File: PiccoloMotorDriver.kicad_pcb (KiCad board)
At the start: 6 copper layers, 55 x 50 mm, 127 parts, among them J1 01x03_MotorTerminal, J11 CAN, J2 Debug, J3 RS485, J4 Conn_01x05, J5 Screw_Terminal_01x02_POWER, J6 Connector, USB-TYPE-C-16P, J7 Conn_01x05, J8 AUX0, J9 AUX0, U1 SP485EEN, U2 XC6210B332MR, U3 XL1509, U4 TJA1050T/CM,118, U5 AS5047D, U6 USBLC6-2SC6, U7 STM32H723VGHx, U8 DRV8316RRGFR, X2 X322516MLB4SI

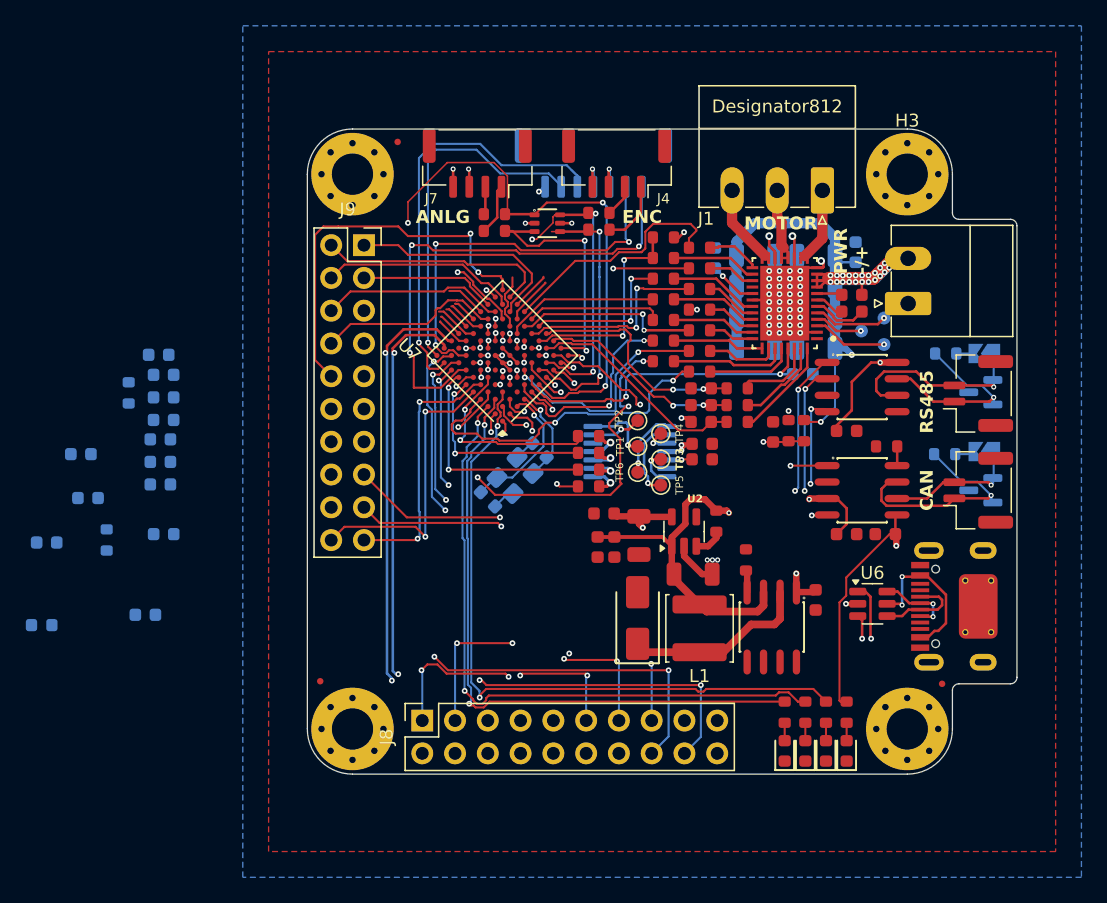
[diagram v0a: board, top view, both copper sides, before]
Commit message: Finished layout, pcba is being tested
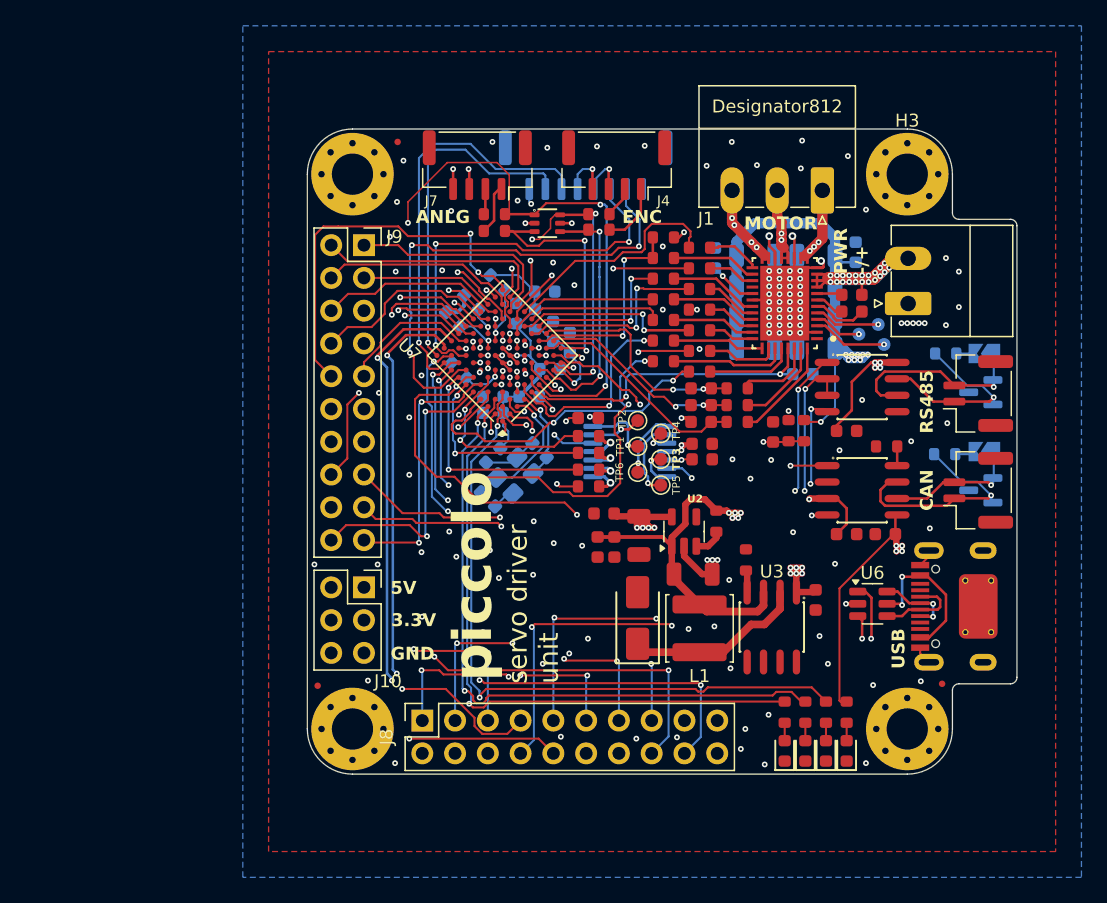
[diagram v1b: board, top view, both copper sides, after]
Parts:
- removed J2: Debug, Connector_JST:JST_GH_SM07B-GHS-TB_1x07-1MP_P1.25mm_Horizontal
- added J10: AUX2, Connector_PinSocket_2.54mm:PinSocket_2x03_P2.54mm_Vertical, F.Cu at (117.4, 110.5)
- added J12: C265111, Connector_JST:JST_GH_SM08B-GHS-TB_1x08-1MP_P1.25mm_Horizontal, B.Cu at (134.6, 77.8)
- C3: moved to F.Cu
- J11: value CAN -> C189893
- J3: value RS485 -> C189893
- J4, J7: value Conn_01x05 -> C225127
- J9: value AUX0 -> AUX1
- moved FB2 45.0 mm to (130.7, 89.8), turned to -90 degrees
- moved C29 39.2 mm to (133.3, 91.5), turned to 90 degrees
- moved C28 38.5 mm to (132.1, 90.7), turned to 90 degrees
- moved C1 37.8 mm to (125.7, 88.5), turned to 135 degrees
- moved C3 34.1 mm to (134.8, 97.4), turned to 0 degrees
- moved C35 33.3 mm to (131.4, 87.6), turned to 0 degrees
- moved C2 30.7 mm to (124.3, 89.8), turned to 135 degrees
- moved C36 30.3 mm to (131.8, 93.6), turned to 0 degrees
- moved R26 30.3 mm to (124.8, 93.7), turned to -45 degrees
- moved R25 29.8 mm to (127.8, 86.9), turned to -45 degrees
- moved C31 29.0 mm to (130.2, 95.8), turned to 0 degrees
- moved C34 27.7 mm to (129.2, 89.3), turned to 90 degrees
- moved C30 25.9 mm to (127.4, 100.3), turned to -135 degrees
- moved C32 25.9 mm to (127.4, 97.0)
- moved C33 25.6 mm to (127.4, 95.8)
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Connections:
- J8 pad 10: /Mcu/PD0 -> /Mcu/PA10
- J8 pad 17: /Mcu/PE11 -> /Mcu/PB15
- J8 pad 2: /Mcu/PE12 -> /Mcu/PB8
- J8 pad 4: /Mcu/PE13 -> /Mcu/PA9
- U7 pad B4: unconnected-(U7-PB8-PadB4) -> /Mcu/PB8
- U7 pad C9: unconnected-(U7-PA9-PadC9) -> /Mcu/PA9
- U7 pad D10: unconnected-(U7-PA10-PadD10) -> /Mcu/PA10
- U7 pad G10: unconnected-(U7-PB15-PadG10) -> /Mcu/PB15
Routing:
- net /Mcu/PC9: track 3.38 -> 67.2 mm, vias 0 -> 1
- net +3.3V: track 61.6 -> 120.4 mm, vias 9 -> 18
- net /Mcu/PE15: track 4.37 -> 60.2 mm, vias 0 -> 3
- net /Mcu/PC6: track 1.90 -> 53.8 mm, vias 0 -> 3
- net /Mcu/PA10: track 0.00 -> 49.9 mm, vias 0 -> 2
- net /Mcu/PB15: track 0.00 -> 49.1 mm, vias 0 -> 1
- net /Mcu/PC7: track 2.08 -> 48.0 mm, vias 0 -> 2
- net /Mcu/PC8: track 2.92 -> 46.2 mm, vias 0 -> 3
- net /Mcu/PA9: track 0.00 -> 42.4 mm, vias 0 -> 2
- net /Mcu/PD5: track 1.61 -> 43.9 mm, vias 1 -> 2
- net /Mcu/PB10: track 3.73 -> 44.7 mm, vias 0 -> 1
- net /Mcu/PD4: track 0.56 -> 39.2 mm, vias 1 -> 2
- net +5V: track 71.3 -> 109.3 mm, vias 5 -> 12
- net /Mcu/PB12: track 2.98 -> 39.9 mm, vias 0 -> 1
- net /Mcu/PB8: track 0.00 -> 30.2 mm, vias 0 -> 1
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- added copper zone on In3.Cu, net GND
- added copper zone on In4.Cu, net GND
- removed copper zone on In4.Cu, net +3.3V
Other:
- board text added: "3.3V"
- board text added: "5V"
- board text added: "CAN Termination"
- board text added: "DEBUG"
- board text added: "ENCODER"
- board text added: "GND"
- board text added: "RS485 Termination"
- board text added: "USB"
- board text added: "piccolo"
- board text added: "servo driver unit"
